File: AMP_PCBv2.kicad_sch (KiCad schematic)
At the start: 36 parts, among them J1 POWER, J2 EBRAKE, J3 MC, J4 STEERING, U1 Teensy4.0, U2 Adafruit_Feather_M0_RFM9x_LoR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

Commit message: Add watchdog timer, USB/UART, power regulators, finish pin connections and add annotations
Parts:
- removed R? (x2): 10K, symbol Device:R_Small_US
- removed U2: Adafruit_Feather_M0_RFM9x_LoRa_Radio, Module:Adafruit_Feather_M0_RFM, symbol MCU_Module:Adafruit_Feather_M0_RFM9x_LoRa_Radio
- removed U?: 74HC157, symbol 74xx:74LS157
- removed U?: 74LS157, symbol 74xx:74LS157
- added C1, C2: 47pF, symbol Device:C_Small
- added C3: 4.7uF, symbol Device:C_Small
- added C4, C5: 100nF, symbol Device:C_Small
- added C8: 10nF, symbol Device:C_Small
- added D1, D2, D3: GN, symbol Device:LED
- added D10, D4, D5, D6, D7: YL, symbol Device:D_Small
- added D11, D12, D13: RD, symbol Device:D_Small
- added D8, D9: YL, symbol Device:LED
- added J5: OLED Breakout, symbol Connector:Conn_01x04_Female
- added JP1: 5VOB, symbol Jumper:SolderJumper_2_Open
- added JP10, JP3, JP4, JP5, JP6, JP7, JP8, JP9: Jumper_3_Open, symbol Jumper:Jumper_3_Open
- added JP11: 0.25s, symbol Jumper:SolderJumper_2_Open
- added JP12: 1s, symbol Jumper:SolderJumper_2_Open
- added JP13: 2s, symbol Jumper:SolderJumper_2_Open
- added JP14: 4s, symbol Jumper:SolderJumper_2_Open
- added JP2: 3V3OB, symbol Jumper:SolderJumper_2_Open
- added JT1, JT3: Conn_01x14_Male, symbol Connector:Conn_01x14_Male
- added JT2: Conn_01x05_Male, symbol Connector:Conn_01x05_Male
- added JT4: Conn_01x01_Male, symbol Connector:Conn_01x01_Male
- added R1: 560, symbol Device:R_US
- added R10: 130, symbol Device:R_US
- added R11, R14, R24: 56, symbol Device:R_US
- added R12, R17, R22, R28, R38: 56, symbol Device:R_Small_US
- added R2, R7: 27, symbol Device:R_Small_US
- added R3, R33, R34, R4: 10K, symbol Device:R_US
- added R31: 15K, symbol Device:R_Small_US
- added R32: 6.2K, symbol Device:R_Small_US
- added R35, R36, R37: 33, symbol Device:R_Small_US
- added R5: 3.3K, symbol Device:R_US
- added R6: 6.2K, symbol Device:R_US
- added R8: 4.7K, symbol Device:R_Small_US
- added R9: 10K, symbol Device:R_Small_US
- added U2: FT234XD, symbol Interface_USB_OTHER:FT234XD
- added U3, U4: LM1117-ADJ, symbol Regulator_Linear:LM1117-ADJ
- added U7: 74HC4060, symbol 74xx_OTHER:74HC4060
- added U8: 74HC00, symbol 74xx:74HC00
- added USB1: USB_B, symbol Connector:USB_B
- gave numbers to parts that had none: 23
- renumbered JX to JX1
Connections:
- net FEATHER_EBRAKE1 is gone; now on net ERR_EBRAKE1: U6.10 (I1c)
- net FEATHER_EBRAKE2 is gone; now on net ERR_EBRAKE2: U6.13 (I1d)
- net FEATHER_FB is gone; now on net ERR_STEERING: U6.6 (I1b)
- net FEATHER_FS1 is gone; now on net ERR_FS1: U5.3 (I1a)
- net FEATHER_FWD is gone; now on net ERR_FWD: U5.6 (I1b)
- net FEATHER_REV is gone; now on net ERR_REV: U5.10 (I1c)
- net FEATHER_STEERING is gone; now on net ERR_FB: U6.3 (I1a)
- net FEATHER_THROTTLE is gone; now on net ERR_THROTTLE: U5.13 (I1d)
- net +12V: now also D1.2 (A), U3.3 (VI), U4.3 (VI)
- net EBRAKE_EN: now also U1.27 (20_A6_TX5_LRCLK1), D10.2 (A), JT3.8 (Pin_8)
- net EBRAKE_IS1: now also U1.28 (21_A7_RX5_BCLK1), JT3.9 (Pin_9)
- net EBRAKE_IS2: now also U1.29 (22_A8_CTX1), JT3.10 (Pin_10)
- net ERR_EBRAKE1: now also JP9.2 (C)
- net ERR_EBRAKE2: now also JP10.2 (C)
- net ERR_FB: now also JP7.2 (C)
- net ERR_FS1: now also JP3.2 (C)
- net ERR_FWD: now also JP4.2 (C)
- net ERR_REV: now also JP5.2 (C)
- net ERR_STEERING: now also JP8.2 (C)
- net ERR_THROTTLE: now also JP6.2 (C)
- net GND: now also U1.1 (GND), U1.17 (GND), U1.32 (GND), C1.2, C2.2, C3.2, C4.2, C5.2, J5.1 (Pin_1), JP10.1 (A), JP3.1 (A), JP4.1 (A), JP5.1 (A), JP6.1 (A), JP7.1 (A), JP8.1 (A), JP9.1 (A), JT1.1 (Pin_1), JT2.3 (Pin_3), JT3.13 (Pin_13), R1.2, R10.2, R11.2, R12.2, R14.2, R17.2, R22.2, R24.2, R28.2, R3.1, R33.2, R34.2, R35.2, R36.2, R37.2, R38.2, R4.1, R9.2, U2.13 (GND), U2.5 (GND), U3.1 (ADJ), U4.1 (ADJ), U7.8 (GND), U8.10, U8.12, U8.13, U8.7 (GND), U8.9, USB1.4 (GND), USB1.5 (Shield)
- net MCU_EBRAKE1: now also U1.10 (8_TX2_IN1), JT1.10 (Pin_10)
- net MCU_EBRAKE2: now also U1.11 (9_OUT1C), JT1.11 (Pin_11)
- net MCU_FB: now also U1.8 (6_OUT1D), U6.2 (I0a), JT1.8 (Pin_8); no longer U6.5 (I0b)
- net MCU_FS1: now also U1.4 (2_OUT2), JT1.4 (Pin_4)
- net MCU_FWD: now also U1.5 (3_LRCLK2), JT1.5 (Pin_5); no longer R13.1
- net MCU_REV: now also U1.6 (4_BCLK2), JT1.6 (Pin_6); no longer R18.1
- net MCU_STEERING: now also U1.9 (7_RX2_OUT1A), U6.5 (I0b), JT1.9 (Pin_9); no longer U6.2 (I0a)
- net MCU_THROTTLE: now also U1.7 (5_IN2), JT1.7 (Pin_7)
- net MUX_EBRAKE1: now also U6.9 (Zc), D11.2 (A)
- net MUX_EBRAKE2: now also U6.12 (Zd), D12.2 (A)
- net MUX_FB: now also U6.4 (Za), D9.2 (A)
- net MUX_FS1: now also R13.1, U5.4 (Za), D4.2 (A); no longer R23.1
- net MUX_FWD: now also R18.1, U5.7 (Zb), D5.2 (A)
- net MUX_REV: now also R23.1, U5.9 (Zc), D6.2 (A)
- net MUX_STEERING: now also U6.7 (Zb), D7.2 (A)
- net MUX_THROTTLE: now also U5.12 (Zd), D8.2 (A)
- net OUT_FS1: now also Q1.2 (D); no longer Q3.2 (D)
- net OUT_FWD: now also Q2.2 (D); no longer Q1.2 (D)
- net OUT_REV: now also Q3.2 (D); no longer Q2.2 (D)
- net at U1.12 (10_CS_MQSR): now also JT1.12 (Pin_12)
- net at U1.13 (11_MOSI_CTX1): now also JT1.13 (Pin_13)
- net at U1.14 (12_MISO_MQSL): now also JT1.14 (Pin_14)
- net at U1.15 (VBAT): now also JT2.1 (Pin_1)
- net at U1.16 (3V3): now also JT2.2 (Pin_2)
- net at U1.18 (PROGRAM): now also JT2.4 (Pin_4)
- net at U1.19 (ON_OFF): now also JT2.5 (Pin_5)
- net RX1: now reaches U1.2 (0_RX1_CRX2_CS1)
- net RX1: now also JT1.2 (Pin_2), U2.7 (TXD)
- net at U1.20 (13_SCK_CRX1_LED): now also JT3.1 (Pin_1)
- net WD_SET: now reaches U1.21 (14_A0_TX3_SPDIF_OUT)
- net WD_SET: now also JP11.2 (B), JP12.2 (B), JP13.2 (B), JP14.2 (B), JT3.2 (Pin_2), R33.1, U8.1
- net WD_RESET: now reaches U1.22 (15_A1_RX3_SPDIF_IN)
- net WD_RESET: now also JT3.3 (Pin_3), R34.1, U7.12 (CLR), U8.5
- net at U1.23 (16_A2_RX4_SCL1): now also JT3.4 (Pin_4)
- net at U1.24 (17_A3_TX4_SDA1): now also JT3.5 (Pin_5)
- net OLED_SDA: now reaches U1.25 (18_A4_SDA0)
- net OLED_SDA: now also J5.4 (Pin_4), JT3.6 (Pin_6)
- net OLED_SCL: now reaches U1.26 (19_A5_SCL0)
- net OLED_SCL: now also J5.3 (Pin_3), JT3.7 (Pin_7)
- net TX1: now reaches U1.3 (1_TX1_CTX2_MISO1)
- net TX1: now also JT1.3 (Pin_3), U2.10 (RXD)
- net at U1.30 (23_A9_CRX1_MCLK1): now also JT3.11 (Pin_11)
- net at U1.31 (3V3): now also JT3.12 (Pin_12)
- net +5V: now reaches U1.33 (VIN)
- net +5V: now also D2.2 (A), J5.2 (Pin_2), JP1.2 (B), JT3.14 (Pin_14), U7.16 (VCC), U8.14 (VCC)
- net at U1.34 (VUSB): now also JT4.1 (Pin_1)
- net FEATHER_SEL renamed WD_SEL
- net WD_SEL: now also D13.2 (A), U8.3, U8.4
- new net: R8.2, R9.1, U2.6 (CBUS0)
- new net: JP13.1 (A), U7.2 (Q13)
- new net: R2.2, U2.1 (USBD-)
- new net: R7.2, U2.12 (USBD+)
- new net: C1.1, R2.1, USB1.3 (D+)
- new net: U8.2, U8.6
- new net: D5.1 (K), R17.1
- new net: D10.1 (K), R38.1
- new net: R3.2, R5.2
- new net: JP1.1 (A), R5.1, U3.2 (VO)
- new net: C2.1, R7.1, USB1.2 (D-)
- new net: JP2.1 (A), R6.1, U4.2 (VO)
- new net: R4.2, R6.2
- new net: D2.1 (K), R10.1
- new net: D12.1 (K), R36.1
- new net: JP12.1 (A), U7.1 (Q12)
- new net: R31.2, U7.10 (CLKO)
- new net: R32.2, U7.11 (CLKI)
- new net: JP11.1 (A), U7.15 (Q10)
- new net: JP14.1 (A), U7.3 (Q14)
- new net: C8.2, U7.9 (CLKO)
- new net: R8.1, USB1.1 (VBUS)
- new net: D4.1 (K), R12.1
- new net: D1.1 (K), R1.1
- new net: D6.1 (K), R22.1
- new net: D13.1 (K), R35.1
- new net: D8.1 (K), R14.1
- new net: C8.1, R31.1, R32.1
- new net: D9.1 (K), R24.1
- new net: D11.1 (K), R37.1
- new net: D3.1 (K), R11.1
- new net: D7.1 (K), R28.1
- new net +3V3: C3.1, C4.1, C5.1, D3.2 (A), JP10.3 (B), JP2.2 (B), JP3.3 (B), JP4.3 (B), JP5.3 (B), JP6.3 (B), JP7.3 (B), JP8.3 (B), JP9.3 (B), U2.2 (RESET), U2.3 (3V3OUT), U2.4 (VCC), U2.9 (VCCIO)
- no-connect marks 4 -> 34
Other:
- note added: "EBRAKE BREAKOUT"
- note added: "MUX CONTROL FOR REMOTE CONTROL AND EMERGENCY STOP"
- note added: "POWER REGULATION"
- note added: "TEENSY"
- note added: "USB/UART BRIDGE"
- note added: "WATCHDOG TIMER AND LATCH"
- note removed: "EBRAKE BREAKOUT CONNECTED TO SEPARATE PCB"
- note removed: "MUX CONTROL FOR REMOTE CONTROL AND EMERGENCY STOP FIRST SET OF MUXES ARE FOR TEENSY/FEATHER SWITCHING SECOND SET OF MUXES ARE FOR FAILURE STATE"
- note removed: "TODO: ADD FTDI Breakout board -NEEDED FOR SERIAL COMMUNICATION WITH JETSON"
- note removed: "TODO: MAYBE ADD A 12VT to 5V LDO for powering the feather"
- moved on the sheet: C6, C7, J1, J2, J3, J4, J6, JX1, Q1, Q2, Q3, Q4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

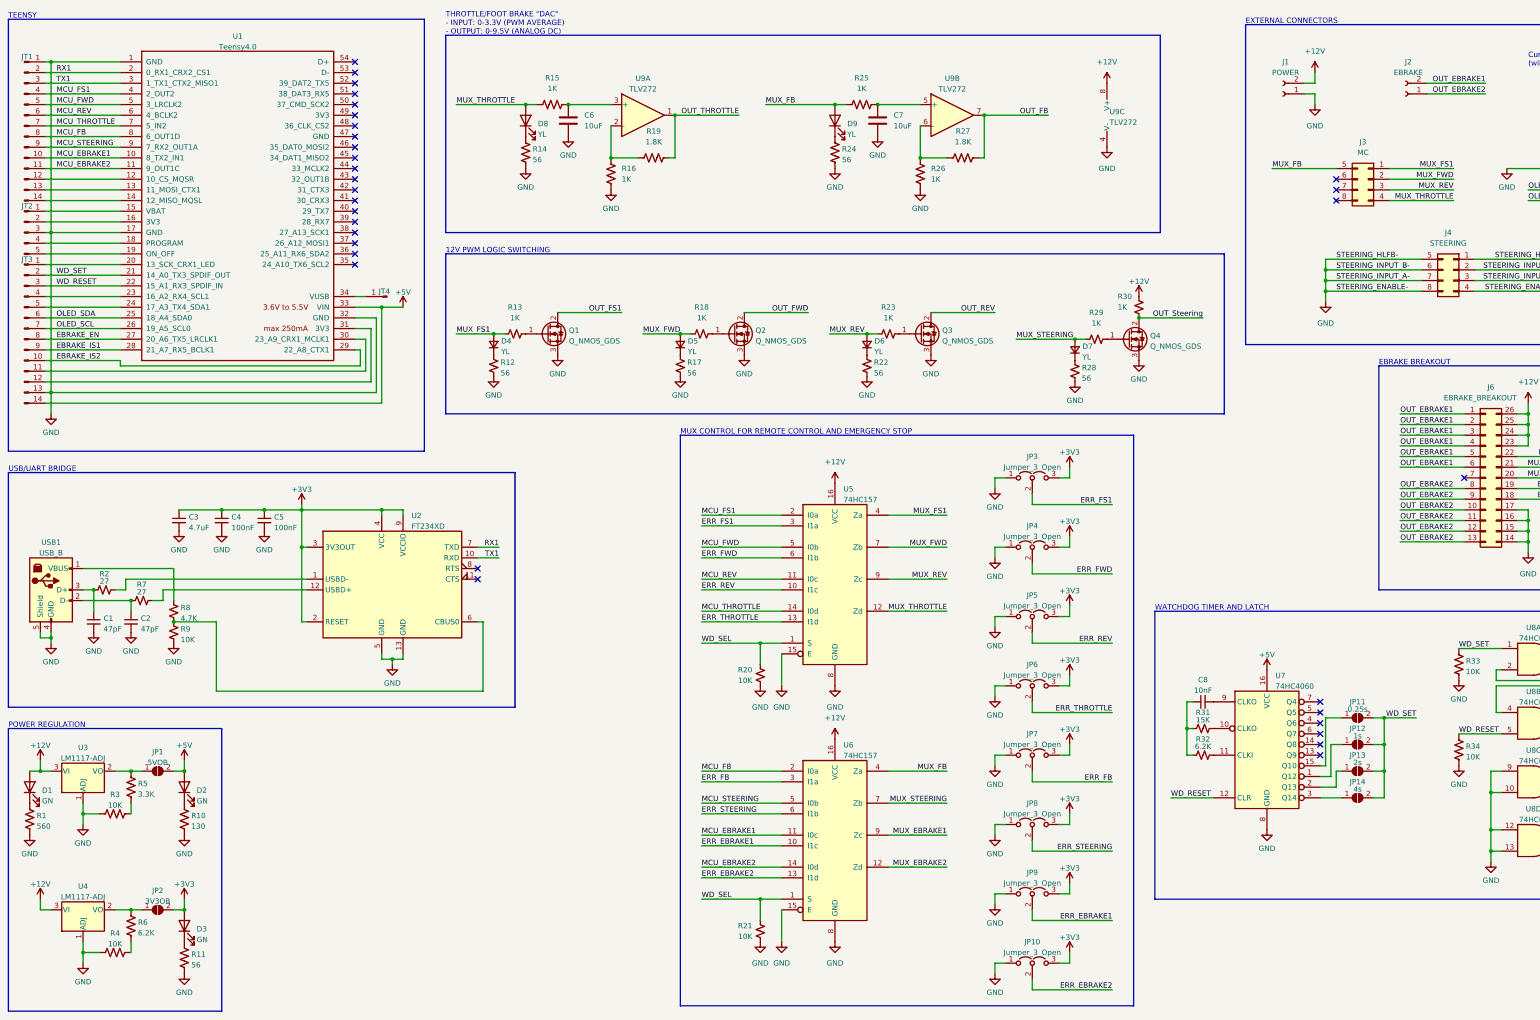
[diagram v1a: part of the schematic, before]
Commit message: Add decoupling capacitors and assign footprints
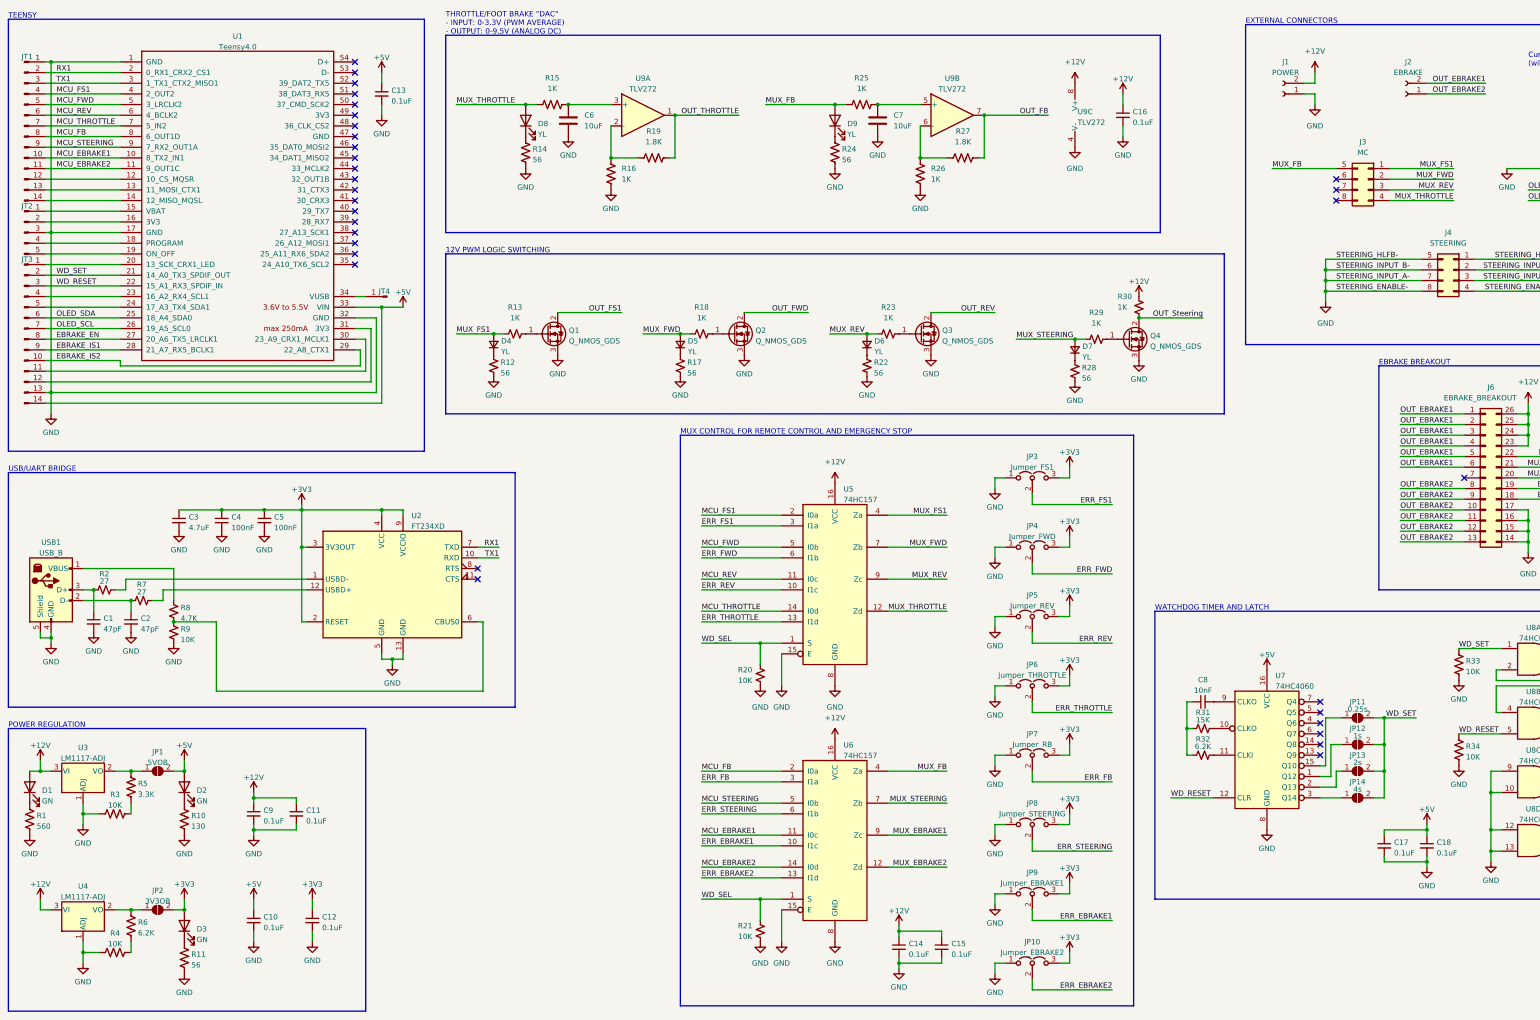
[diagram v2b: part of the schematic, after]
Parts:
- added C10, C11, C12, C13, C14, C15, C16, C17, C18, C9: 0.1uF, Capacitor_SMD:C_0805_2012Metric_Pad1.18x1.45mm_HandSolder, symbol Device:C_Small
- C1, C2, C3, C4, C5, C6, C7, C8: footprint (none) -> Capacitor_SMD:C_0805_2012Metric_Pad1.18x1.45mm_HandSolder
- D1, D10, D11, D12, D13, D2, D3, D4, D5, D6, D7, D8, D9: footprint (none) -> LED_THT:LED_D5.0mm
- J1, J2: footprint (none) -> Connector_Molex:Molex_Mini-Fit_Jr_5566-02A_2x01_P4.20mm_Vertical
- J3, J4: footprint (none) -> Connector_Molex:Molex_Mini-Fit_Jr_5566-08A_2x04_P4.20mm_Vertical
- J5: footprint (none) -> Connector_PinHeader_2.54mm:PinHeader_1x04_P2.54mm_Vertical
- J6: footprint (none) -> AMP:AMP_Brake_Controller_Breakout
- JP1, JP11, JP12, JP13, JP14, JP2: footprint (none) -> Jumper:SolderJumper-2_P1.3mm_Open_TrianglePad1.0x1.5mm
- JP10: value Jumper_3_Open -> Jumper_EBRAKE2; footprint (none) -> Connector_PinHeader_2.54mm:PinHeader_1x03_P2.54mm_Vertical
- JP3: value Jumper_3_Open -> Jumper_FS1; footprint (none) -> Connector_PinHeader_2.54mm:PinHeader_1x03_P2.54mm_Vertical
- JP4: value Jumper_3_Open -> Jumper_FWD; footprint (none) -> Connector_PinHeader_2.54mm:PinHeader_1x03_P2.54mm_Vertical
- JP5: value Jumper_3_Open -> Jumper_REV; footprint (none) -> Connector_PinHeader_2.54mm:PinHeader_1x03_P2.54mm_Vertical
- JP6: value Jumper_3_Open -> Jumper_THROTTLE; footprint (none) -> Connector_PinHeader_2.54mm:PinHeader_1x03_P2.54mm_Vertical
- JP7: value Jumper_3_Open -> Jumper_RB; footprint (none) -> Connector_PinHeader_2.54mm:PinHeader_1x03_P2.54mm_Vertical
- JP8: value Jumper_3_Open -> Jumper_STEERING; footprint (none) -> Connector_PinHeader_2.54mm:PinHeader_1x03_P2.54mm_Vertical
- JP9: value Jumper_3_Open -> Jumper_EBRAKE1; footprint (none) -> Connector_PinHeader_2.54mm:PinHeader_1x03_P2.54mm_Vertical
- JT1, JT3: footprint (none) -> Connector_PinHeader_2.54mm:PinHeader_1x14_P2.54mm_Vertical
- JT2: footprint (none) -> Connector_PinHeader_2.54mm:PinHeader_1x05_P2.54mm_Vertical
- JT4: footprint (none) -> Connector_PinHeader_2.54mm:PinHeader_1x01_P2.54mm_Vertical
- JX1: footprint (none) -> Connector_Molex:Molex_KK-254_AE-6410-04A_1x04_P2.54mm_Vertical
- Q1, Q2, Q3, Q4: footprint (none) -> Package_TO_SOT_THT:TO-251-3_Vertical
- R1, R10, R11, R12, R13, R14, R15, R16, R17, R18, R19, R2, R20, R21, R22, R23, R24, R25, R26, R27, R28, R29, R3, R30, R31, R32, R33, R34, R35, R36, R37, R38, R4, R5, R6, R7, R8, R9: footprint (none) -> Resistor_SMD:R_0805_2012Metric_Pad1.20x1.40mm_HandSolder
- U2: footprint (none) -> Package_DFN_QFN:DFN-12-1EP_3x3mm_P0.5mm_EP1.6x2.5mm
- U3, U4: footprint (none) -> Package_TO_SOT_THT:TO-220-3_Vertical
- U5, U6, U7: footprint (none) -> Package_DIP:DIP-16_W7.62mm
- U8: footprint (none) -> Package_DIP:DIP-14_W7.62mm
- U9: footprint (none) -> Package_DIP:DIP-8_W7.62mm
- USB1: footprint (none) -> Connector_USB:USB_B_TE_5787834_Vertical
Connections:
- net +12V: now also C11.1, C14.1, C15.1, C16.1, C9.1
- net +3V3: now also C12.1
- net +5V: now also C10.1, C13.1, C17.1, C18.1
- net GND: now also C10.2, C11.2, C12.2, C13.2, C14.2, C15.2, C16.2, C17.2, C18.2, C9.2
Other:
- moved on the sheet: U9C

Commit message: Change OLED screen footprint
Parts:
- J5: footprint Connector_PinHeader_2.54mm:PinHeader_1x04_P2.54mm_Vertical -> Connector_PinSocket_2.54mm:PinSocket_1x04_P2.54mm_Vertical
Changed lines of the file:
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@@
       (effects (font (size 1.27 1.27)) (justify left))
     )
-    (property "Footprint" "Connector_PinHeader_2.54mm:PinHeader_1x04_P2.54mm_Vertical" (id 2) (at 394.97 54.61 0)
+    (property "Footprint" "Connector_PinSocket_2.54mm:PinSocket_1x04_P2.54mm_Vertical" (id 2) (at 394.97 54.61 0)
       (effects (font (size 1.27 1.27)) hide)
     )
@@
     )
     (path "/6e096d07-50b1-4d38-a410-59f9bd13afff"
-      (reference "J5") (unit 1) (value "OLED Breakout") (footprint "Connector_PinHeader_2.54mm:PinHeader_1x04_P2.54mm_Vertical")
+      (reference "J5") (unit 1) (value "OLED Breakout") (footprint "Connector_PinSocket_2.54mm:PinSocket_1x04_P2.54mm_Vertical")
     )
     (path "/ff78fa55-4dad-4168-9c36-443a87175a9c"

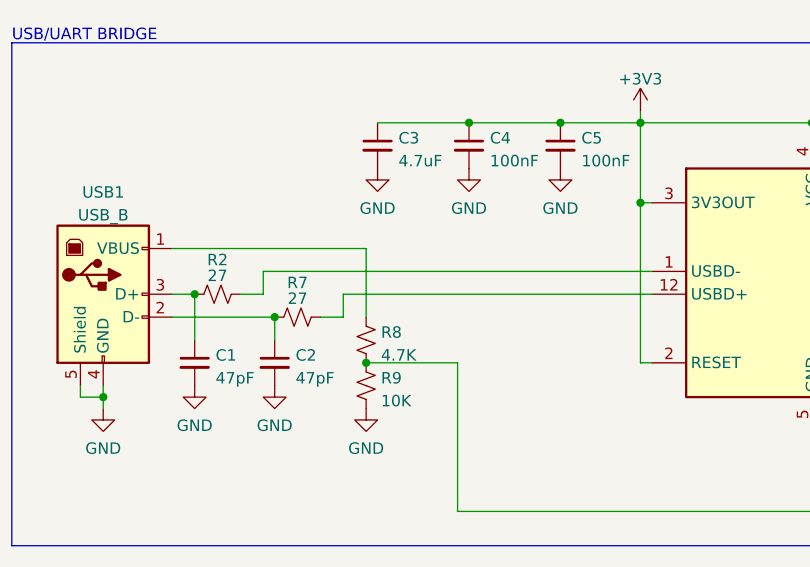
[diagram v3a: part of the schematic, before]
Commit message: Route differential pair for USB connection
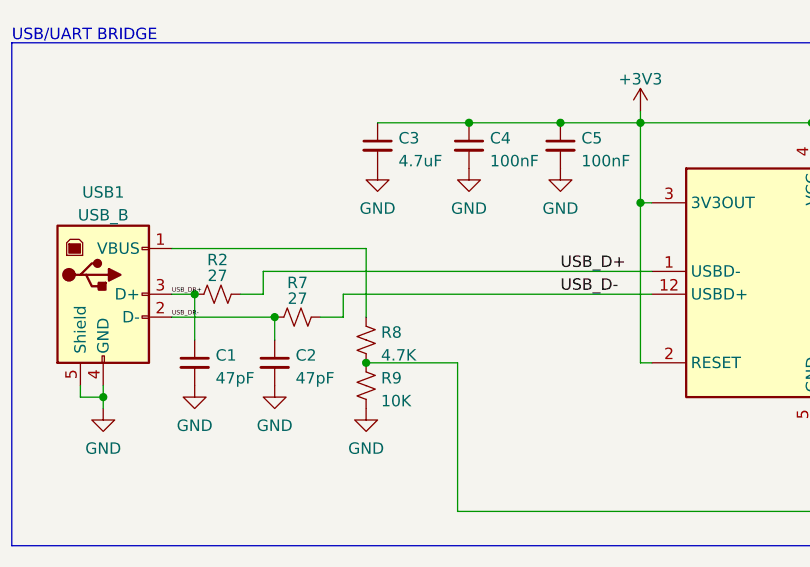
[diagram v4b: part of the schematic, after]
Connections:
- net USB_D+: now reaches R2.2, U2.1 (USBD-)
- net USB_D-: now reaches R7.2, U2.12 (USBD+)
- net USB_DR+: now reaches C1.1, R2.1, USB1.3 (D+)
- net USB_DR-: now reaches C2.1, R7.1, USB1.2 (D-)
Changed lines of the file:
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@@
     (effects (font (size 1.27 1.27)) (justify right bottom))
+  )
+  (label "USB_DR-" (at 35.56 154.94 0)
+    (effects (font (size 0.5 0.5)) (justify left bottom))
   )
   (label "RX1" (at 29.21 29.21 0)
@@
   )
   (label "MCU_REV" (at 182.88 149.86 0)
+    (effects (font (size 1.27 1.27)) (justify left bottom))
+  )
+  (label "USB_D+" (at 78.74 149.86 0)
     (effects (font (size 1.27 1.27)) (justify left bottom))
   )
@@
     (effects (font (size 1.27 1.27)) (justify left bottom))
   )
+  (label "USB_DR+" (at 35.56 152.4 0)
+    (effects (font (size 0.5 0.5)) (justify left bottom))
+  )
   (label "MCU_THROTTLE" (at 182.88 157.48 0)
     (effects (font (size 1.27 1.27)) (justify left bottom))
@@
     (effects (font (size 1.27 1.27)) (justify right bottom))
   )
+  (label "USB_D-" (at 78.74 152.4 0)
+    (effects (font (size 1.27 1.27)) (justify left bottom))
+  )
   (label "MUX_THROTTLE" (at 124.46 36.83 0)

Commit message: Add LoRa module and extra decoupling capacitors
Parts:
- added C19, C20: 10uF, Capacitor_SMD:C_0805_2012Metric_Pad1.18x1.45mm_HandSolder, symbol Device:C_Small
- added U10: RFM9x, RF_Module_OTHER:RFM9x_Adafruit, symbol RF_Module_OTHER:RMF9x
- C10, C12: value 0.1uF -> 10uF
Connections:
- net +12V: now also C19.1, C20.1
- net +3V3: now also U10.1 (VIN); no longer C12.1
- net +5V: no longer C10.1
- net GND: now also C19.2, C20.2, U10.2 (GND)
- net LORA_CS: now reaches JT1.12 (Pin_12), U1.12 (10_CS_MQSR)
- net LORA_CS: now also U10.8 (CS)
- net LORA_MOSI: now reaches JT1.13 (Pin_13), U1.13 (11_MOSI_CTX1)
- net LORA_MOSI: now also U10.7 (MOSI)
- net LORA_MISO: now reaches JT1.14 (Pin_14), U1.14 (12_MISO_MQSL)
- net LORA_MISO: now also U10.6 (MISO)
- net at JP1.1 (A), R5.1, U3.2 (VO): now also C10.1
- net at JP2.1 (A), R6.1, U4.2 (VO): now also C12.1
- net LORA_SCK: now reaches JT3.1 (Pin_1), U1.20 (13_SCK_CRX1_LED)
- net LORA_SCK: now also U10.5 (SCK)
- new net LORA_INT: U10.4 (G0)
- new net LORA_RST: U10.9 (RST)
- no-connect marks 34 -> 40
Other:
- note added: "LORA MODULE (SPI)"
- moved on the sheet: C1, C10, C12, C13, C14, C15, C16, C17, C18, C2, C3, C4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
